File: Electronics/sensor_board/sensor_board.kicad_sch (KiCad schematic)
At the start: 10 parts, among them U1 L7805

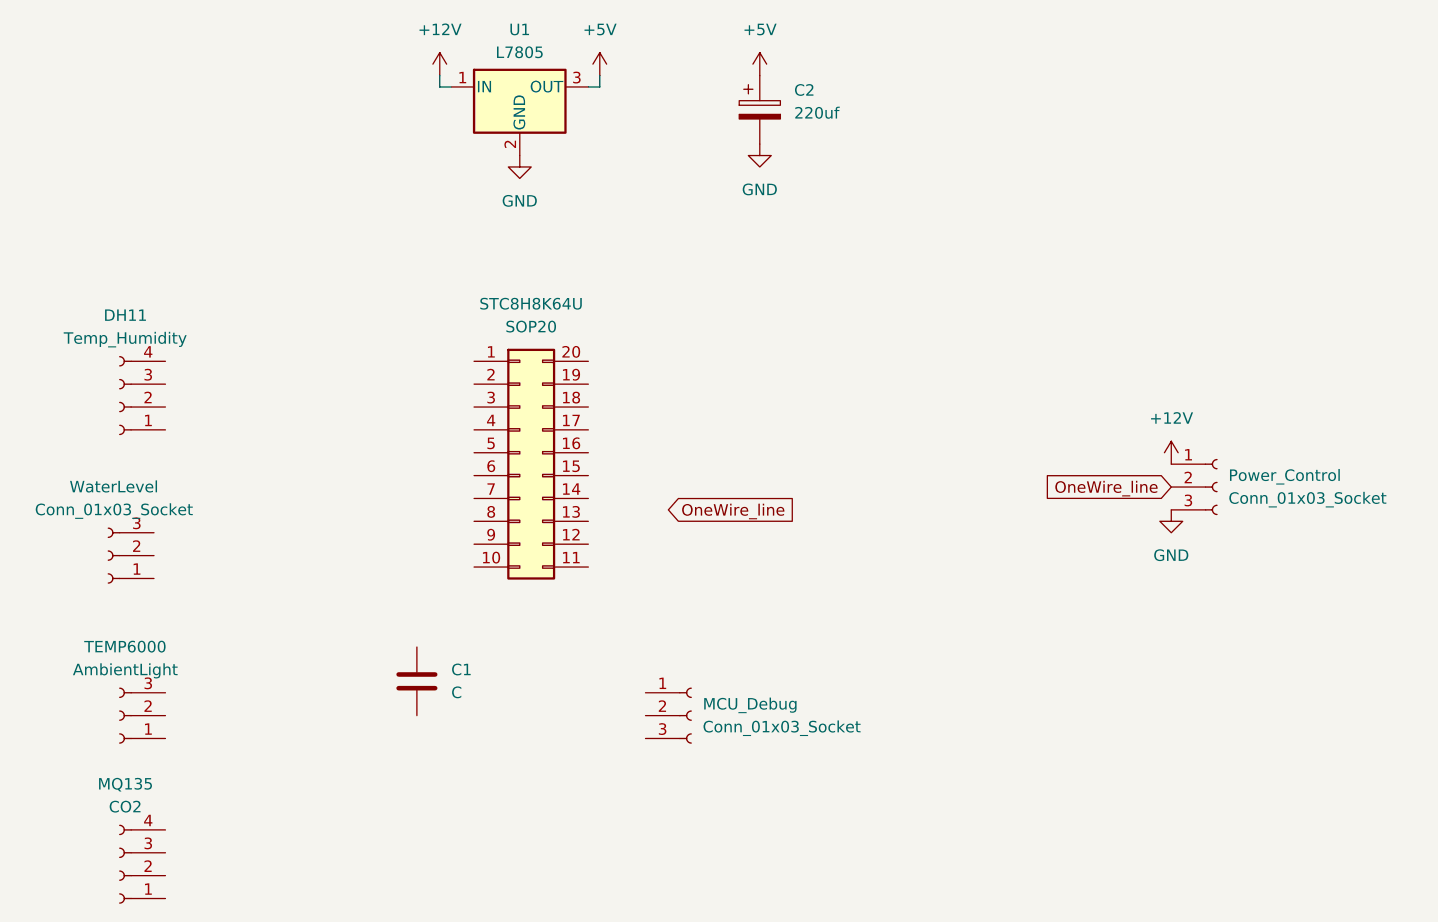
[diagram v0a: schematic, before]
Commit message: finished sensor board PCB
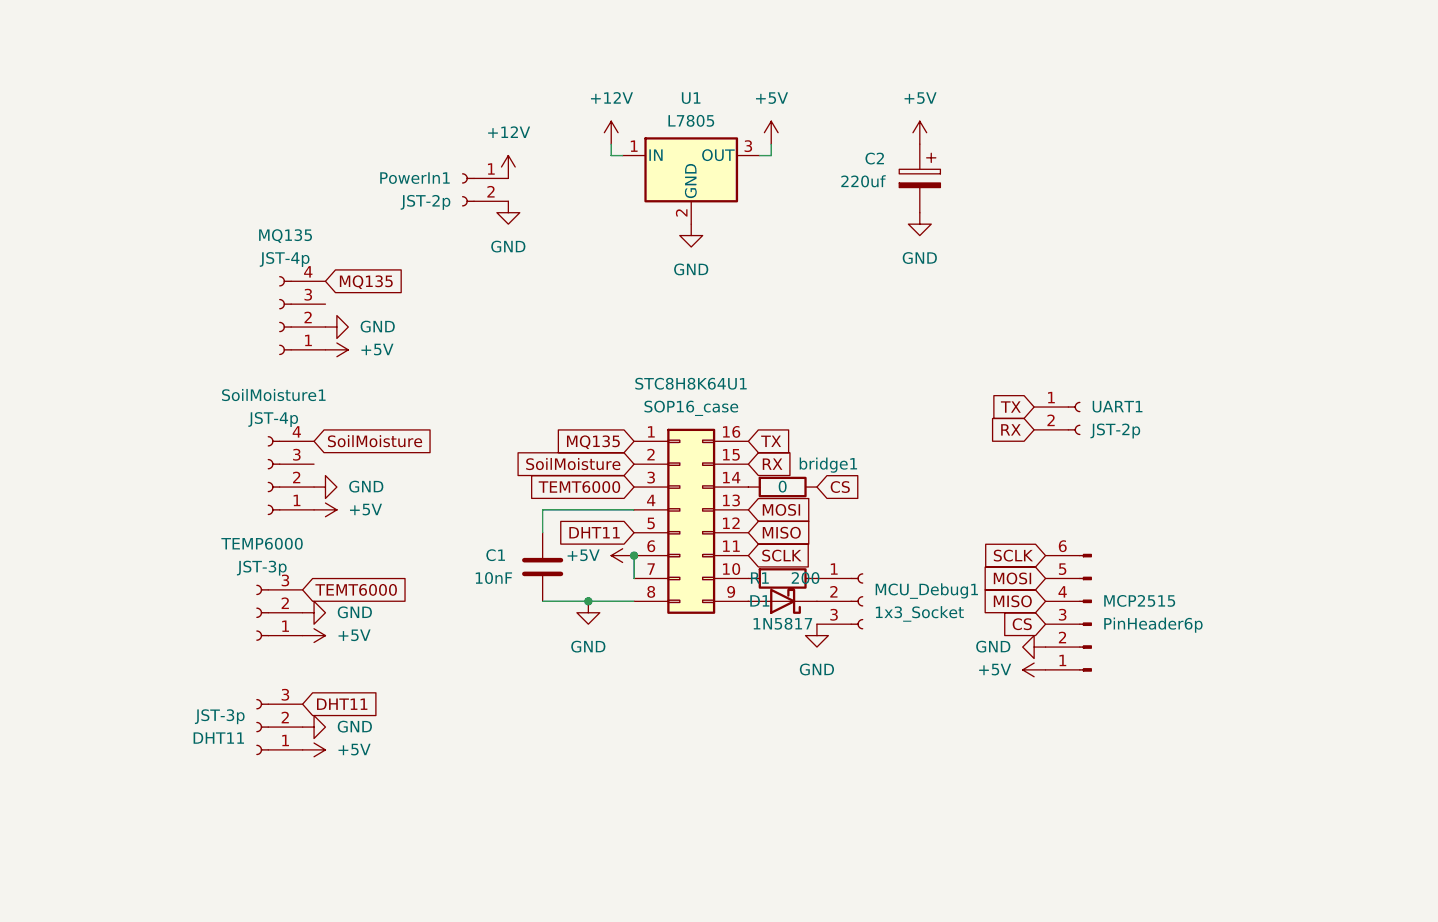
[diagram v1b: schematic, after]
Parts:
- removed DH11: Temp_Humidity, Connector_JST:JST_EH_B4B-EH-A_1x04_P2.50mm_Vertical, symbol Connector:Conn_01x04_Socket
- removed Power_Control, WaterLevel: Conn_01x03_Socket, Connector_JST:JST_EH_B3B-EH-A_1x03_P2.50mm_Vertical, symbol Connector:Conn_01x03_Socket
- removed STC8H8K64U: SOP20, Package_DIP:DIP-20_W7.62mm_LongPads, symbol Connector_Generic:Conn_02x10_Counter_Clockwise
- added D1: 1N5817, Diode_THT:D_DO-41_SOD81_P10.16mm_Horizontal, symbol Diode:1N5817
- added DHT11: JST-3p, Connector_JST:JST_EH_B3B-EH-A_1x03_P2.50mm_Vertical, symbol Connector:Conn_01x03_Socket
- added MCP2515: PinHeader6p, Connector_PinSocket_2.54mm:PinSocket_1x06_P2.54mm_Vertical, symbol Connector:Conn_01x06_Pin
- added PowerIn1, UART1: JST-2p, Connector_JST:JST_EH_B2B-EH-A_1x02_P2.50mm_Vertical, symbol Connector:Conn_01x02_Socket
- added R1: 200, Resistor_THT:R_Axial_DIN0207_L6.3mm_D2.5mm_P7.62mm_Horizontal, symbol Device:R
- added STC8H8K64U1: SOP16_case, Package_DIP:DIP-16_W7.62mm_LongPads, symbol Connector_Generic:Conn_02x08_Counter_Clockwise
- added SoilMoisture1: JST-4p, Connector_JST:JST_EH_B4B-EH-A_1x04_P2.50mm_Vertical, symbol Connector:Conn_01x04_Socket
- added bridge1: 0, Resistor_THT:R_Axial_DIN0207_L6.3mm_D2.5mm_P7.62mm_Horizontal, symbol Device:R
- C1: value C -> 10nF; footprint (none) -> Capacitor_THT:C_Disc_D5.0mm_W2.5mm_P5.00mm
- C2: footprint (none) -> Capacitor_THT:CP_Radial_D6.3mm_P2.50mm
- MCU_Debug1: renamed from MCU_Debug; value Conn_01x03_Socket -> 1x3_Socket; footprint Connector_JST:JST_EH_B3B-EH-A_1x03_P2.50mm_Vertical -> Connector_PinSocket_2.54mm:PinSocket_1x03_P2.54mm_Vertical
- MQ135: value CO2 -> JST-4p
- TEMP6000: value AmbientLight -> JST-3p
- U1: footprint (none) -> Package_TO_SOT_THT:TO-220-3_Vertical
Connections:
- net +12V: now also PowerIn1.1 (Pin_1)
- net +5V: now also MQ135.1 (Pin_1), TEMP6000.1 (Pin_1), DHT11.1 (Pin_1), MCP2515.1 (Pin_1), STC8H8K64U1.6 (Pin_6), STC8H8K64U1.7 (Pin_7), SoilMoisture1.1 (Pin_1)
- net GND: now also C1.2, MCU_Debug1.3 (Pin_3), MQ135.2 (Pin_2), TEMP6000.2 (Pin_2), DHT11.2 (Pin_2), MCP2515.2 (Pin_2), PowerIn1.2 (Pin_2), STC8H8K64U1.8 (Pin_8), SoilMoisture1.2 (Pin_2)
- net TEMT6000: now reaches TEMP6000.3 (Pin_3)
- net TEMT6000: now also STC8H8K64U1.3 (Pin_3)
- net at C1.1: now also STC8H8K64U1.4 (Pin_4)
- net MQ135: now reaches MQ135.4 (Pin_4)
- net MQ135: now also STC8H8K64U1.1 (Pin_1)
- net at MCU_Debug1.1 (Pin_1): now also R1.1
- net at MCU_Debug1.2 (Pin_2): now also D1.1 (K)
- new net: R1.2, STC8H8K64U1.10 (Pin_10)
- new net: STC8H8K64U1.14 (Pin_14), bridge1.2
- new net: D1.2 (A), STC8H8K64U1.9 (Pin_9)
- new net CS: MCP2515.3 (Pin_3), bridge1.1
- new net DHT11: DHT11.3 (Pin_3), STC8H8K64U1.5 (Pin_5)
- new net MISO: MCP2515.4 (Pin_4), STC8H8K64U1.12 (Pin_12)
- new net MOSI: MCP2515.5 (Pin_5), STC8H8K64U1.13 (Pin_13)
- new net RX: STC8H8K64U1.15 (Pin_15), UART1.2 (Pin_2)
- new net SCLK: MCP2515.6 (Pin_6), STC8H8K64U1.11 (Pin_11)
- new net SoilMoisture: STC8H8K64U1.2 (Pin_2), SoilMoisture1.4 (Pin_4)
- new net TX: STC8H8K64U1.16 (Pin_16), UART1.1 (Pin_1)
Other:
- moved on the sheet: C1, C2, MCU_Debug1, MQ135, TEMP6000, U1
